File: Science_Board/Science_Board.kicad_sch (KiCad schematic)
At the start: 32 parts, among them J1 Conn_01x02, J10 Conn_01x02, J11 Conn_01x03, J12 Conn_01x03, J13 Conn_01x03, J14 Conn_01x03, J15 Conn_01x03, J16 Conn_01x03, J17 Conn_01x03, J18 Conn_01x03, J19 Conn_01x02, J2 RJ45_LED_Shielded, J20 Molex_Megafit_02, J22 Molex_Megafit_02, J5 Conn_01x02, J6 Conn_01x04, J7 Conn_01x03, J8 Conn_01x03, J9 Conn_01x02, U5 PCA9685BS

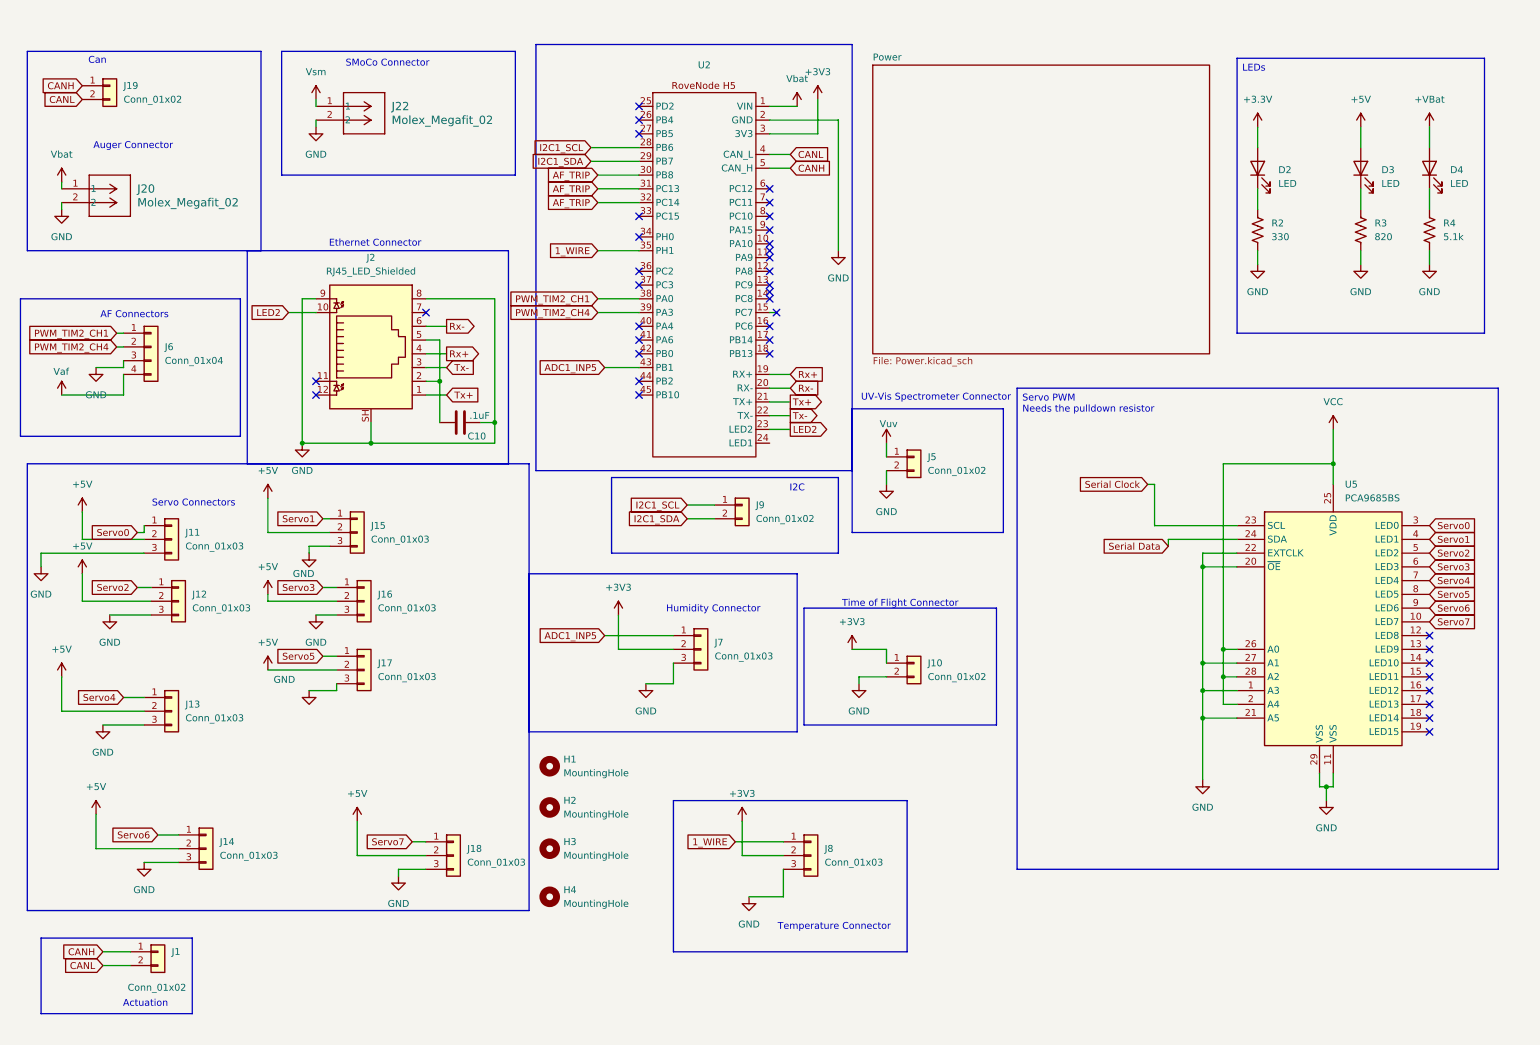
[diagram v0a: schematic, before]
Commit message: Fixed Reverse Voltage Protection, small formatting fixes
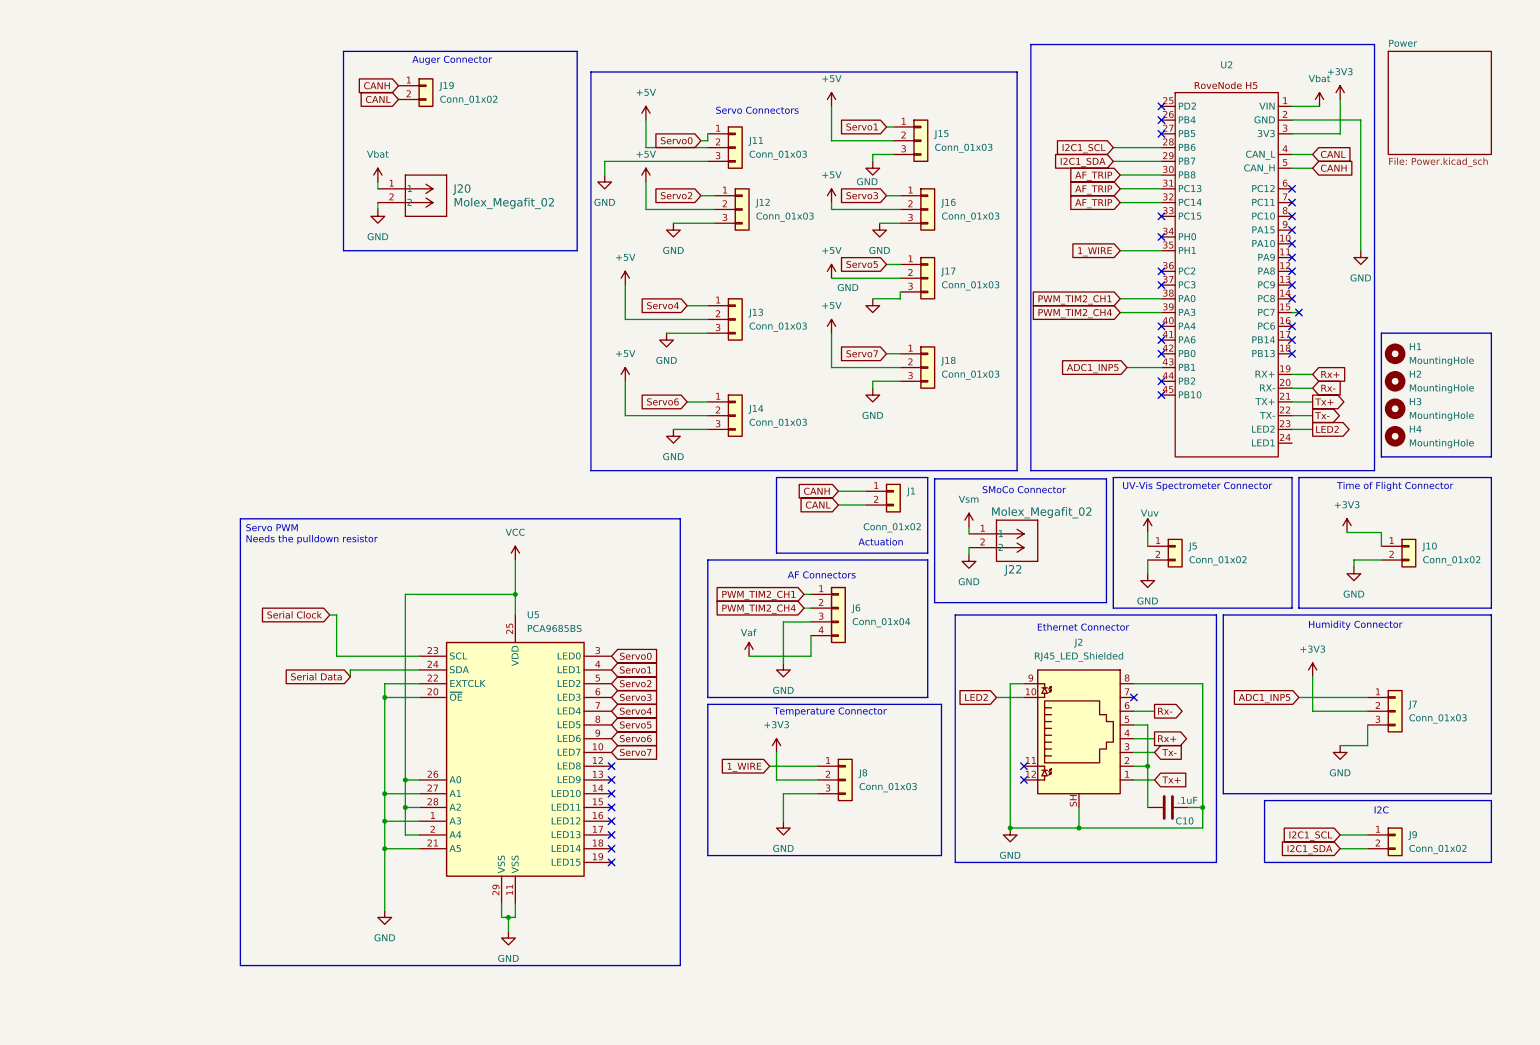
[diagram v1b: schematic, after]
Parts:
- removed D2, D3, D4: LED, Diode_SMD:D_0603_1608Metric_Pad1.05x0.95mm_HandSolder, symbol Device:LED
- removed R2: 330, Package_DIP:DIP-8_W7.62mm, symbol Device:R_US
- removed R3: 820, Package_DIP:DIP-8_W7.62mm, symbol Device:R_US
- removed R4: 5.1k, Package_DIP:DIP-8_W7.62mm, symbol Device:R_US
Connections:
- no-connect marks 38 -> 36
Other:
- note removed: "Can"
- moved on the sheet: C10, H1, H2, H3, H4, J1, J10, J11, J12, J13, J14, J15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

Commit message: Created the 11 buttons and the switch
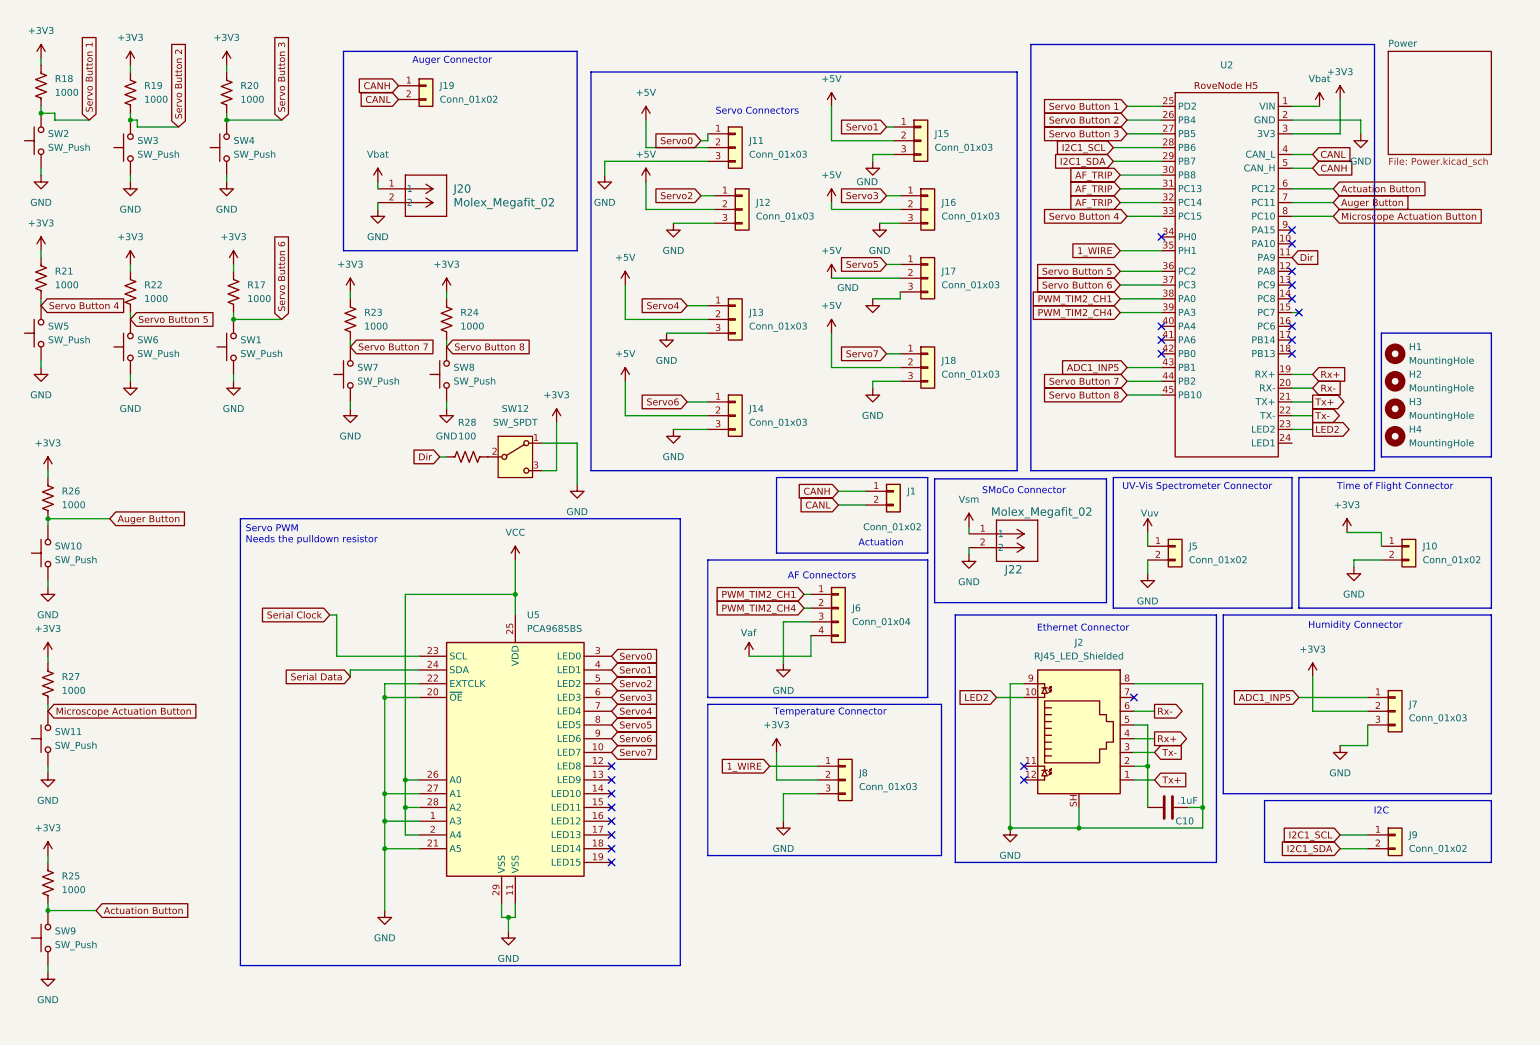
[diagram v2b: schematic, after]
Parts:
- added R17, R18, R19, R20, R21, R22, R23, R24, R25, R26, R27: 1000, Package_DIP:DIP-8_W7.62mm, symbol Device:R_US
- added R28: 100, Package_DIP:DIP-8_W7.62mm, symbol Device:R_US
- added SW1, SW10, SW11, SW2, SW3, SW4, SW5, SW6, SW7, SW8, SW9: SW_Push, Package_DIP:DIP-8_W7.62mm, symbol Switch:SW_Push
- added SW12: SW_SPDT, Button_Switch_THT:SW_NKK_GW12LJP, symbol Switch:SW_SPDT
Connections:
- net +3V3: now also R17.1, R18.1, R19.1, R20.1, R21.1, R22.1, R23.1, R24.1, R25.1, R26.1, R27.1, SW12.3 (C)
- net GND: now also SW1.1, SW10.1, SW11.1, SW12.1 (A), SW2.1, SW3.1, SW4.1, SW5.1, SW6.1, SW7.1, SW8.1, SW9.1
- net Dir: now reaches U2.11 (PA9)
- net Dir: now also R28.1
- net Servo Button 1: now reaches U2.25 (PD2)
- net Servo Button 1: now also R18.2, SW2.2
- net Servo Button 2: now reaches U2.26 (PB4)
- net Servo Button 2: now also R19.2, SW3.2
- net Servo Button 3: now reaches U2.27 (PB5)
- net Servo Button 3: now also R20.2, SW4.2
- net Servo Button 4: now reaches U2.33 (PC15)
- net Servo Button 4: now also R21.2, SW5.2
- net Servo Button 5: now reaches U2.36 (PC2)
- net Servo Button 5: now also R22.2, SW6.2
- net Servo Button 6: now reaches U2.37 (PC3)
- net Servo Button 6: now also R17.2, SW1.2
- net Servo Button 7: now reaches U2.44 (PB2)
- net Servo Button 7: now also R23.2, SW7.2
- net Servo Button 8: now reaches U2.45 (PB10)
- net Servo Button 8: now also R24.2, SW8.2
- net Actuation Button: now reaches U2.6 (PC12)
- net Actuation Button: now also R25.2, SW9.2
- net Auger Button: now reaches U2.7 (PC11)
- net Auger Button: now also R26.2, SW10.2
- net Microscope Actuation Button: now reaches U2.8 (PC10)
- net Microscope Actuation Button: now also R27.2, SW11.2
- new net: R28.2, SW12.2 (B)
- no-connect marks 36 -> 24

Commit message: added support for microscope light
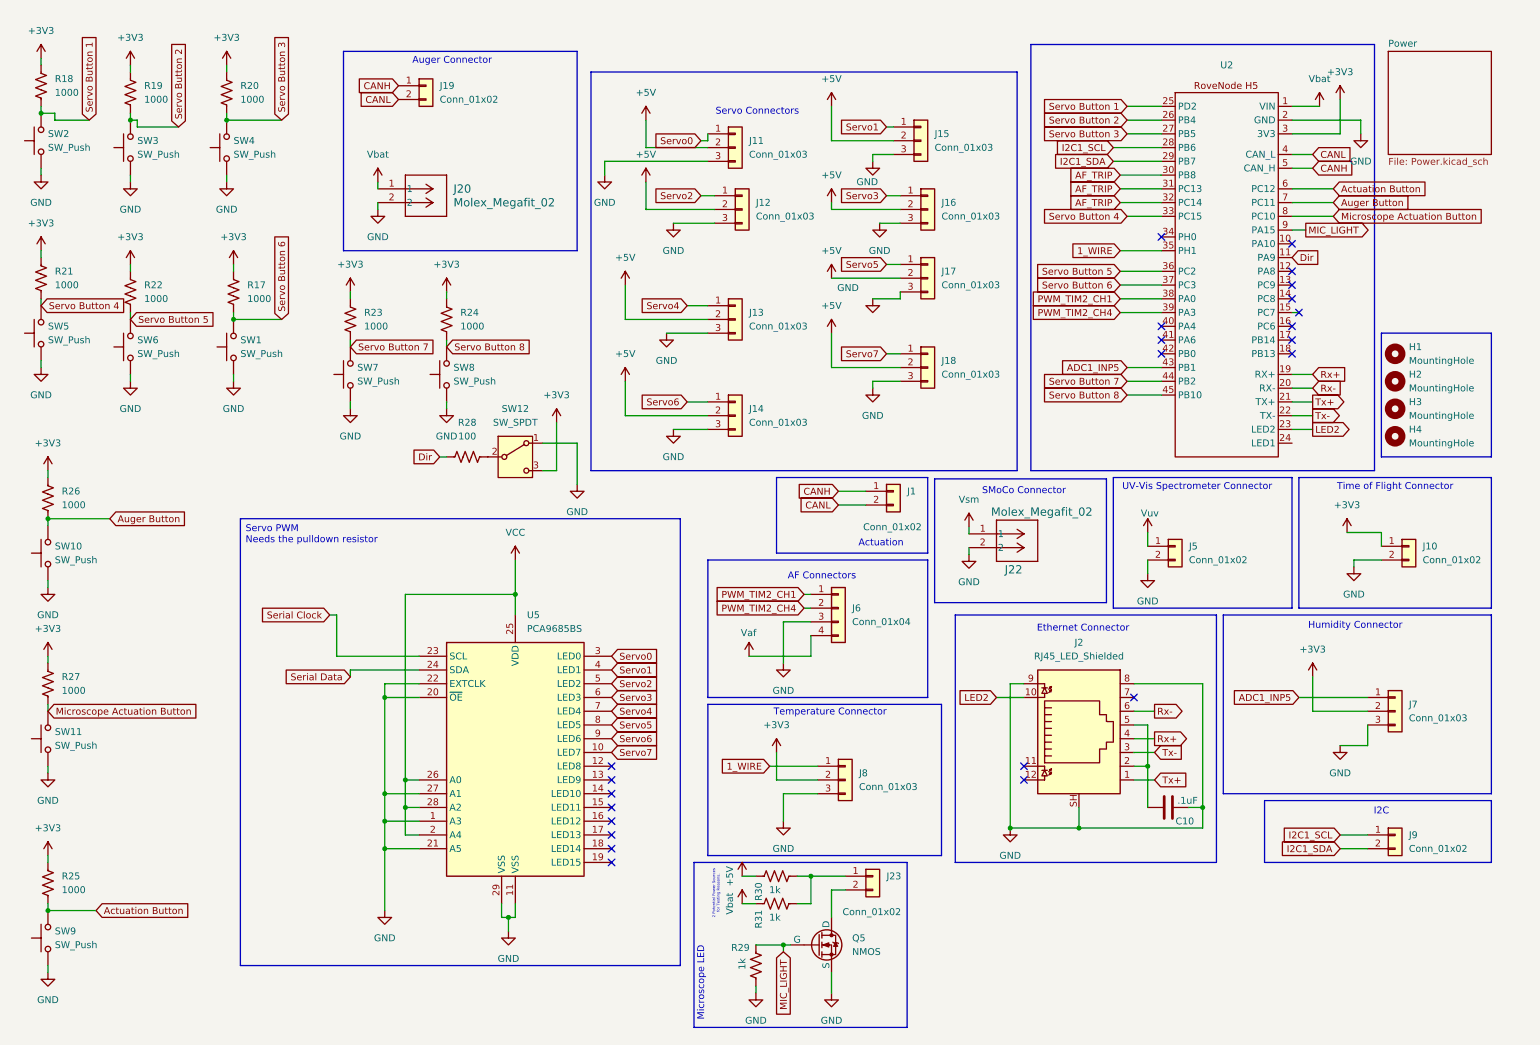
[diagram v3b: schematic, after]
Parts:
- added J23: Conn_01x02, Connector_JST:JST_PH_B2B-PH-K_1x02_P2.00mm_Vertical, symbol Connector_Generic:Conn_01x02
- added Q5: NMOS, symbol Simulation_SPICE:NMOS
- added R29, R30, R31: 1k, Package_DIP:DIP-8_W7.62mm, symbol Device:R_US
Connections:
- net +5V: now also R30.1
- net GND: now also Q5.3 (S), R29.2
- net Vbat: now also R31.1
- net MIC_LIGHT: now reaches U2.9 (PA15)
- net MIC_LIGHT: now also Q5.2 (G), R29.1
- new net: J23.2 (Pin_2), Q5.1 (D)
- new net: J23.1 (Pin_1), R30.2, R31.2
- no-connect marks 24 -> 23
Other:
- note added: "2 Potential Power Sources for Testing Reasons."
- note added: "Microscope LED"
